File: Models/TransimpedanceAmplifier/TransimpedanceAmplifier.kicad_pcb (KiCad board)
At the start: 2 copper layers, 107 parts, among them J1 Conn_01x02_Socket, J10 Conn_01x02_Pin, J11 Conn_01x24_Socket, J14 Conn_01x24_Socket, J2 Conn_01x02_Socket, J3 Conn_01x03_Pin, J4 Conn_01x02_Pin, J5 Conn_01x02_Pin, J6 Conn_01x02_Pin, J7 Conn_01x02_Pin, J8 Conn_01x02_Pin, J9 Conn_01x02_Pin, Q1 Q_PNP, Q2 Q_NPN, U1 LM7905, -5V, 5%, U10 DAC81401, U11 ISO7641FM, U12 ISO7641FM, U13 ADS8699, U2 LM7805, 5V, 5%, U3 OPA828, U4 AD8615, U5 OP37GPZ, U6 LM7915, -15V, 5%, U7 LM7815, 15V, 5%, U8 LM7805, 5V, 5%, U9 TLV76133, 3.3V, 1%

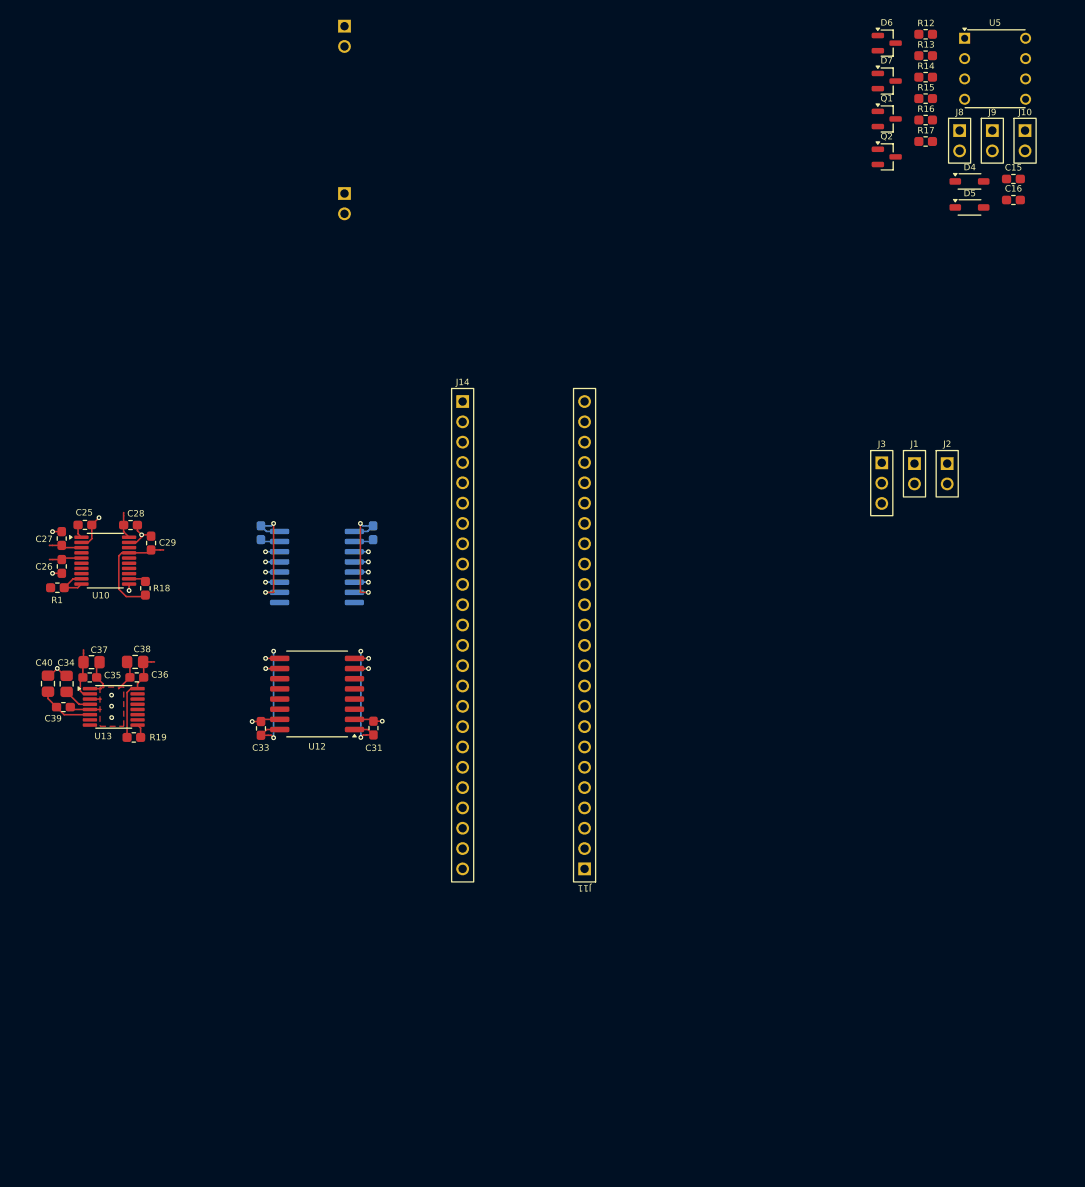
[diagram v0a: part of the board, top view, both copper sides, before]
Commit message: Resolved some of the OP37's auxiliary components
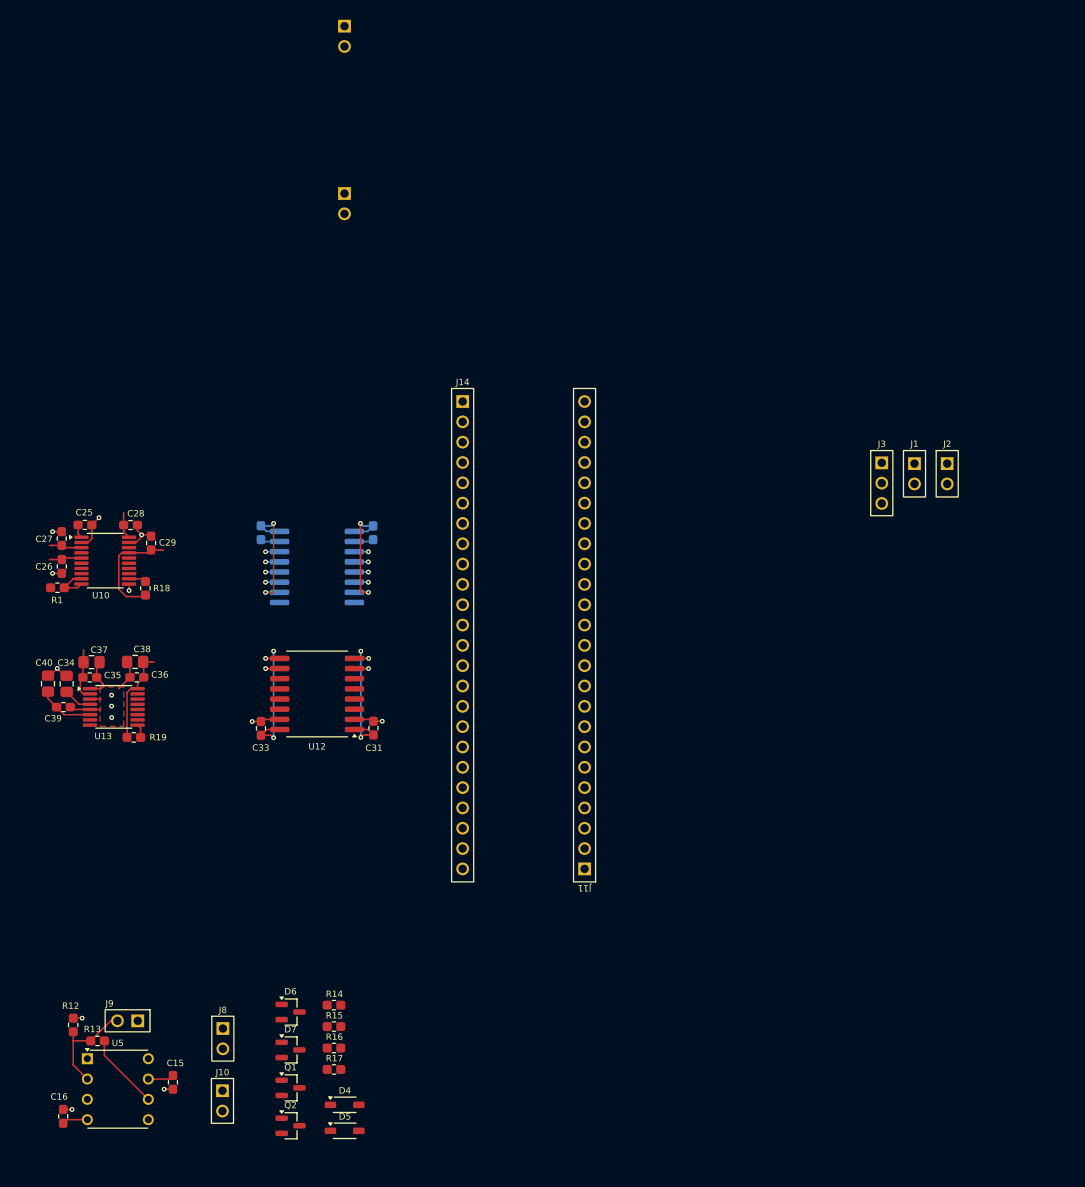
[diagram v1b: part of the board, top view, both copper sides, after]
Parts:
- moved U5 168.2 mm to (108.4, 151.0)
- moved C16 165.0 mm to (101.6, 154.4), turned to 90 degrees
- moved R12 163.4 mm to (102.8, 143.0), turned to -90 degrees
- moved R13 160.9 mm to (105.9, 145.0)
- moved J10 156.4 mm to (121.5, 152.5)
- moved C15 154.2 mm to (115.3, 150.2), turned to -90 degrees
- moved J9 154.2 mm to (109.6, 142.5), turned to -90 degrees
- moved J8 145.2 mm to (121.6, 144.7)
- moved D6 142.2 mm to (130.0, 141.4)
- moved D7 142.2 mm to (130.0, 146.1)
- moved Q1 142.2 mm to (130.0, 150.9)
- moved Q2 142.2 mm to (130.0, 155.6)
- moved D4 139.4 mm to (136.8, 153.0)
- moved D5 139.4 mm to (136.8, 156.3)
- moved R15 137.6 mm to (135.4, 143.2)
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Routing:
- net Net-(J9-Pin_2): track 0.00 -> 13.2 mm
- net /TIA_TwoStage/Output: track 0.00 -> 9.58 mm
- net GND: track 121.2 -> 124.5 mm, vias 22 -> 25
- net /TIA_TwoStage/PostAmplifier/V+: track 0.00 -> 3.27 mm
- net /TIA_TwoStage/PostAmplifier/V-: track 0.00 -> 3.20 mm

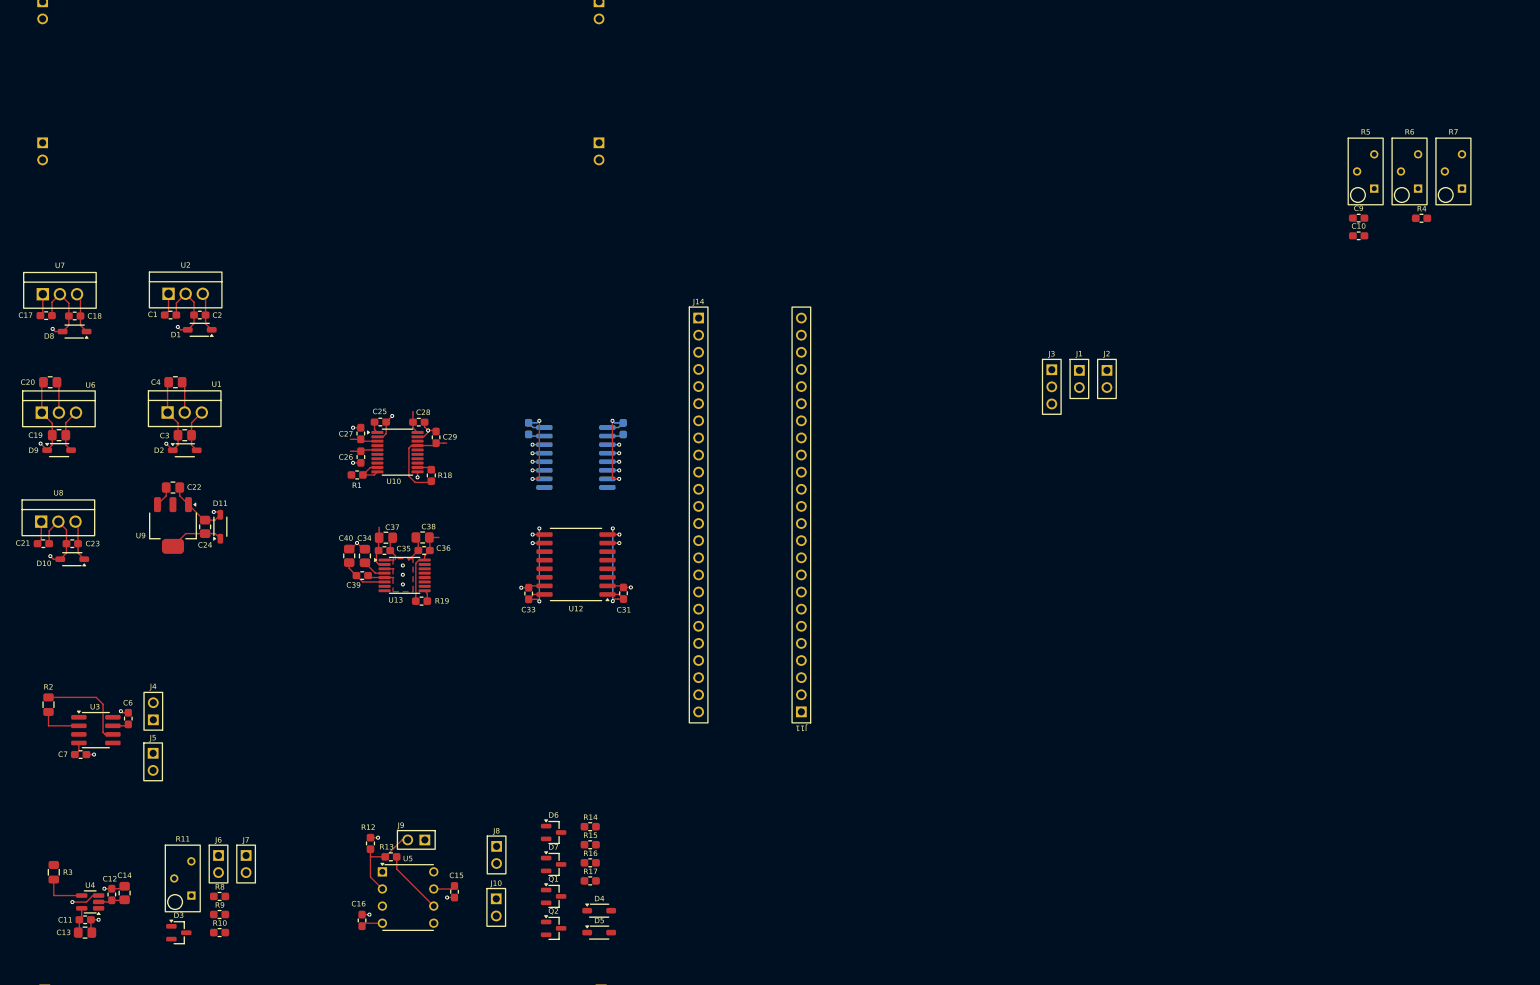
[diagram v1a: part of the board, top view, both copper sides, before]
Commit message: Sorting out the high-level arrangement of subsystems
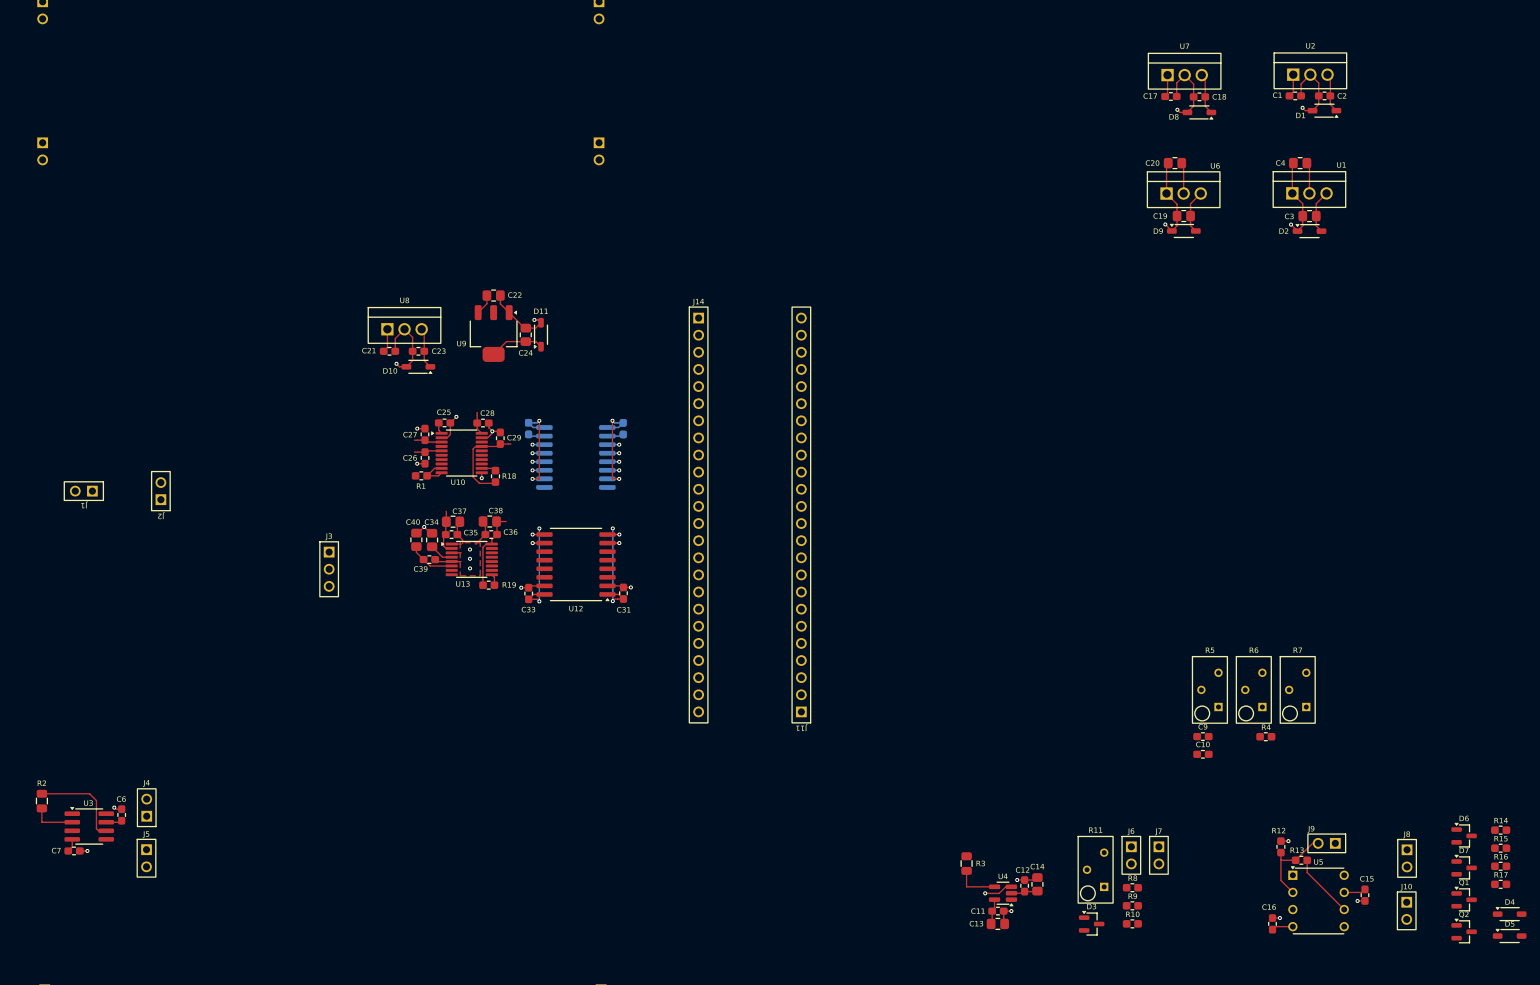
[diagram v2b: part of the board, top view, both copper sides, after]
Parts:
- moved C3 170.0 mm to (242.2, 50.0)
- moved D1 170.0 mm to (244.4, 34.3)
- moved D2 170.0 mm to (242.2, 52.2)
- moved C1 170.0 mm to (240.0, 32.1)
- moved C17 170.0 mm to (221.6, 32.2)
- moved C18 170.0 mm to (225.8, 32.3)
- moved C19 170.0 mm to (223.5, 50.0)
- moved C2 170.0 mm to (244.4, 32.1)
- moved C20 170.0 mm to (222.2, 42.1)
- moved C4 170.0 mm to (240.8, 42.1)
- moved D8 170.0 mm to (225.8, 34.6)
- moved D9 170.0 mm to (223.5, 52.2)
- moved U2 170.0 mm to (242.3, 29.0)
- moved U6 170.0 mm to (223.5, 46.6)
- moved U7 170.0 mm to (223.6, 29.0)
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
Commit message: Now at approximately 17 in^2 of board size
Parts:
- moved J10 234.3 mm to (23.4, 176.0)
- moved R14 234.3 mm to (37.3, 164.0)
- moved R15 234.3 mm to (37.3, 166.7)
- moved R16 234.3 mm to (37.3, 169.4)
- moved R17 234.3 mm to (37.3, 172.1)
- moved D4 234.3 mm to (38.7, 176.5)
- moved D5 234.3 mm to (38.7, 179.7)
- moved D6 234.3 mm to (31.9, 164.9)
- moved D7 234.3 mm to (31.9, 169.6)
- moved Q1 234.3 mm to (31.9, 174.4)
- moved Q2 234.3 mm to (31.9, 179.1)
- moved J8 234.3 mm to (23.4, 168.2)
- moved C3 215.7 mm to (26.6, 40.4)
- moved C4 215.7 mm to (25.3, 32.5)
- moved D2 215.7 mm to (26.6, 42.6)
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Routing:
- net Net-(J9-Pin_2): track 13.2 -> 18.8 mm
- net GND: track 124.5 -> 123.4 mm, vias 25 -> 24
- net /TIA_TwoStage/Output: track 9.58 -> 8.80 mm

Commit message: 15 in^2 at this point, sufficient to finalize the general power topology
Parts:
- moved C17 160.6 mm to (132.9, 130.9)
- moved U7 160.6 mm to (134.9, 127.7)
- moved C18 160.6 mm to (137.1, 130.9)
- moved D8 160.6 mm to (137.1, 133.2)
- moved C19 158.0 mm to (118.7, 68.0)
- moved C20 158.0 mm to (117.4, 60.1)
- moved D9 158.0 mm to (118.7, 70.2)
- moved U6 158.0 mm to (118.7, 64.6)
- moved C3 82.9 mm to (104.7, 68.3)
- moved D2 82.9 mm to (104.7, 70.5)
- moved U1 82.9 mm to (104.7, 64.9)
- moved C4 82.9 mm to (103.3, 60.4)
- moved Q2 79.7 mm to (98.2, 135.0), turned to 90 degrees
- moved D5 79.3 mm to (98.9, 128.2), turned to 90 degrees
- moved D4 74.7 mm to (95.6, 128.2), turned to 90 degrees
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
